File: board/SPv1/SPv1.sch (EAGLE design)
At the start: 72 parts, among them IC1 S34ML0XG1, IC2 F55[0/1]X---PT48, IC3 S34ML0XG1, IC4 74LS14D, IC5 F55[0/1]X---PT48, IC6 74LS14D, Q1 12MHz, Q2 12MHz

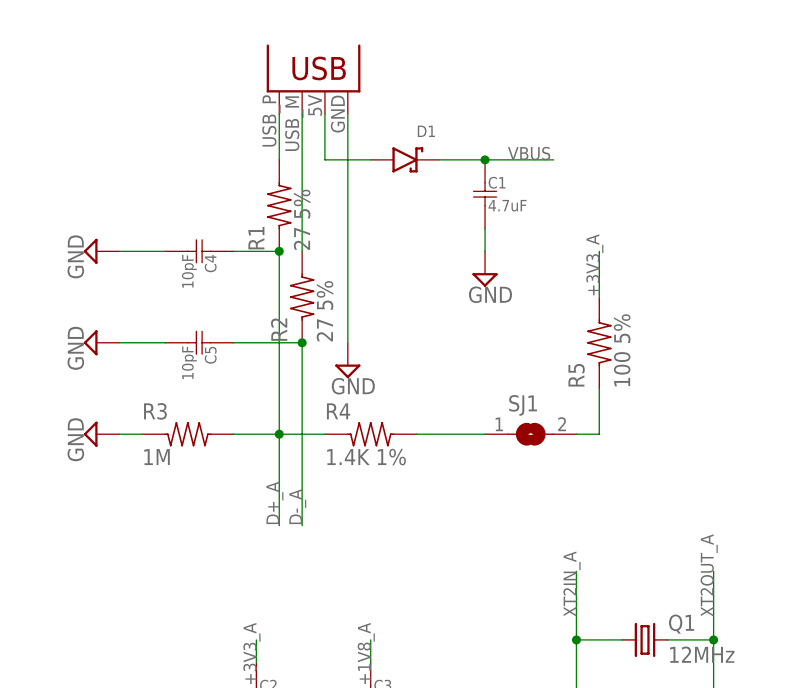
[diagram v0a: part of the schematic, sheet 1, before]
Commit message: fixes to board (connector; PUR line)
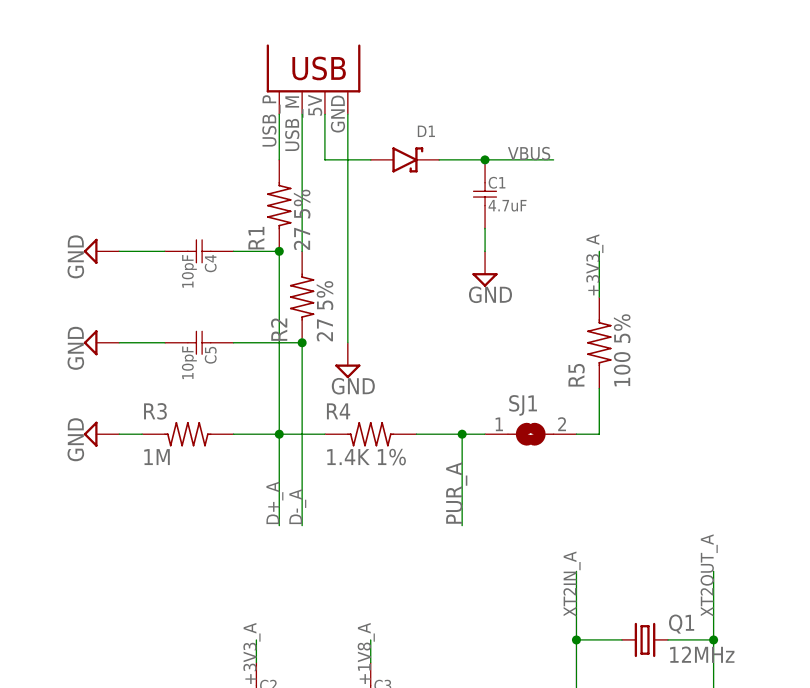
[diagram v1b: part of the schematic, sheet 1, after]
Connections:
- removed net N$11: R4.2, SJ1.1
- removed net N$32: R11.2, SJ2.1
- net PUR_A: now also R4.2, SJ1.1
- net PUR_B: now also R11.2, SJ2.1
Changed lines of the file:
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@@
-</segment>
-<segment>
-<pinref part="JP1" gate="G$1" pin="GND"/>
-<pinref part="SUPPLY5" gate="GND" pin="GND"/>
-<wire x1="129.54" y1="104.14" x2="129.54" y2="129.54" width="0.1524" layer="91"/>
 </segment>
 <segment>
@@
 <pinref part="U$1" gate="G$1" pin="A1"/>
 <wire x1="17.78" y1="33.02" x2="22.86" y2="33.02" width="0.1524" layer="91"/>
+</segment>
+<segment>
+<pinref part="JP1" gate="G$1" pin="GND"/>
+<pinref part="SUPPLY5" gate="GND" pin="GND"/>
+<wire x1="129.54" y1="129.54" x2="129.54" y2="104.14" width="0.1524" layer="91"/>
 </segment>
 </net>
@@
 <label x="76.2" y="93.98" size="1.4224" layer="95"/>
 </segment>
+<segment>
+<pinref part="SJ1" gate="1" pin="1"/>
+<pinref part="R4" gate="G$1" pin="2"/>
+<wire x1="144.78" y1="93.98" x2="142.24" y2="93.98" width="0.1524" layer="91"/>
+<wire x1="142.24" y1="93.98" x2="137.16" y2="93.98" width="0.1524" layer="91"/>
+<wire x1="142.24" y1="93.98" x2="142.24" y2="83.82" width="0.1524" layer="91"/>
+<junction x="142.24" y="93.98"/>
+<label x="142.24" y="83.82" size="1.778" layer="95" rot="R90"/>
+</segment>
 </net>
 <net name="TDO_A" class="0">
@@
 </segment>
 </net>
-<net name="N$11" class="0">
-<segment>
-<pinref part="SJ1" gate="1" pin="1"/>
-<pinref part="R4" gate="G$1" pin="2"/>
-<wire x1="144.78" y1="93.98" x2="137.16" y2="93.98" width="0.1524" layer="91"/>
-</segment>
-</net>
 <net name="SW_A" class="0">
 <segment>
@@
 <net name="N$33" class="0">
 <segment>
+<pinref part="D1" gate="G$1" pin="ANODE"/>
 <pinref part="JP1" gate="G$1" pin="VBUS"/>
-<wire x1="127" y1="129.54" x2="127" y2="124.46" width="0.1524" layer="91"/>
-<pinref part="D1" gate="G$1" pin="ANODE"/>
 <wire x1="132.08" y1="124.46" x2="127" y2="124.46" width="0.1524" layer="91"/>
+<wire x1="127" y1="124.46" x2="127" y2="129.54" width="0.1524" layer="91"/>
 </segment>
 </net>
@@
 </segment>
 <segment>
-<pinref part="JP2" gate="G$1" pin="GND"/>
-<pinref part="SUPPLY20" gate="GND" pin="GND"/>
-<wire x1="111.76" y1="68.58" x2="111.76" y2="93.98" width="0.1524" layer="91"/>
-</segment>
-<segment>
 <pinref part="C13" gate="G$1" pin="1"/>
 <pinref part="SUPPLY21" gate="GND" pin="GND"/>
@@
 <pinref part="U$2" gate="G$1" pin="A1"/>
 <wire x1="0" y1="-2.54" x2="5.08" y2="-2.54" width="0.1524" layer="91"/>
+</segment>
+<segment>
+<pinref part="JP2" gate="G$1" pin="GND"/>
+<pinref part="SUPPLY20" gate="GND" pin="GND"/>
+<wire x1="111.76" y1="93.98" x2="111.76" y2="68.58" width="0.1524" layer="91"/>
 </segment>
 </net>
@@
 <pinref part="SJ2" gate="1" pin="2"/>
 <wire x1="139.7" y1="58.42" x2="137.16" y2="58.42" width="0.1524" layer="91"/>
-</segment>
-</net>
-<net name="N$32" class="0">
-<segment>
-<pinref part="SJ2" gate="1" pin="1"/>
-<pinref part="R11" gate="G$1" pin="2"/>
-<wire x1="127" y1="58.42" x2="119.38" y2="58.42" width="0.1524" layer="91"/>
 </segment>
 </net>
@@
 <label x="58.42" y="58.42" size="1.4224" layer="95"/>
 </segment>
+<segment>
+<pinref part="SJ2" gate="1" pin="1"/>
+<pinref part="R11" gate="G$1" pin="2"/>
+<wire x1="127" y1="58.42" x2="124.46" y2="58.42" width="0.1524" layer="91"/>
+<wire x1="124.46" y1="58.42" x2="119.38" y2="58.42" width="0.1524" layer="91"/>
+<wire x1="124.46" y1="58.42" x2="124.46" y2="48.26" width="0.1524" layer="91"/>
+<junction x="124.46" y="58.42"/>
+<label x="124.46" y="48.26" size="1.778" layer="95" rot="R90"/>
+</segment>
 </net>
 <net name="D+_B" class="0">
@@
 </segment>
 </net>
-<net name="N$40" class="0">
-<segment>
-<pinref part="JP2" gate="G$1" pin="VBUS"/>
-<wire x1="109.22" y1="93.98" x2="109.22" y2="88.9" width="0.1524" layer="91"/>
-<pinref part="D2" gate="G$1" pin="ANODE"/>
-<wire x1="114.3" y1="88.9" x2="109.22" y2="88.9" width="0.1524" layer="91"/>
-</segment>
-</net>
 <net name="INTER_RXB_TXA" class="0">
 <segment>
@@
 </segment>
 </net>
+<net name="N$40" class="0">
+<segment>
+<pinref part="D2" gate="G$1" pin="ANODE"/>
+<pinref part="JP2" gate="G$1" pin="VBUS"/>
+<wire x1="114.3" y1="88.9" x2="109.22" y2="88.9" width="0.1524" layer="91"/>
+<wire x1="109.22" y1="88.9" x2="109.22" y2="93.98" width="0.1524" layer="91"/>
+</segment>
+</net>
